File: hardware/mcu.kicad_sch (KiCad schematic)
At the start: 26 parts, among them J5 Conn_ARM_JTAG_SWD_10, SW3 SW_Push, U2 EFR32FG28A122F1024GM48-A, U20 USBLC6-2P6, U21 USBLC6-2P6, X1 HF_Crystal, Y1 LF_Crystal

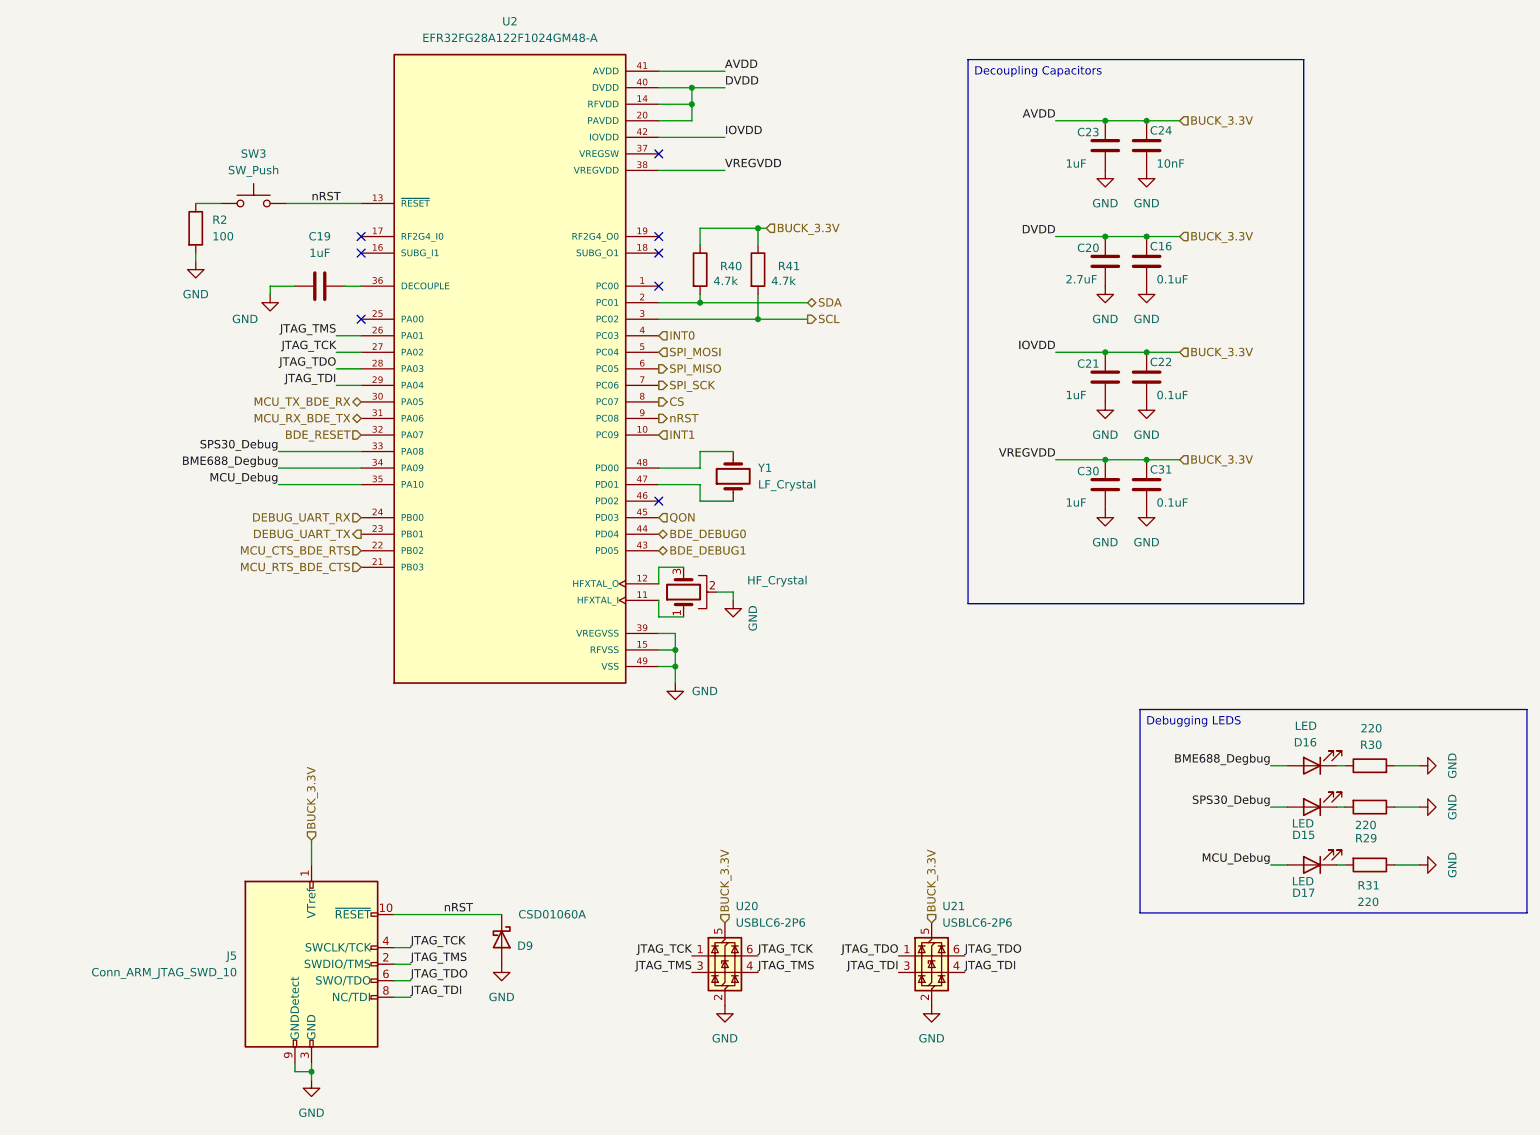
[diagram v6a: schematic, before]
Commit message: Replaced 3.3V symbol
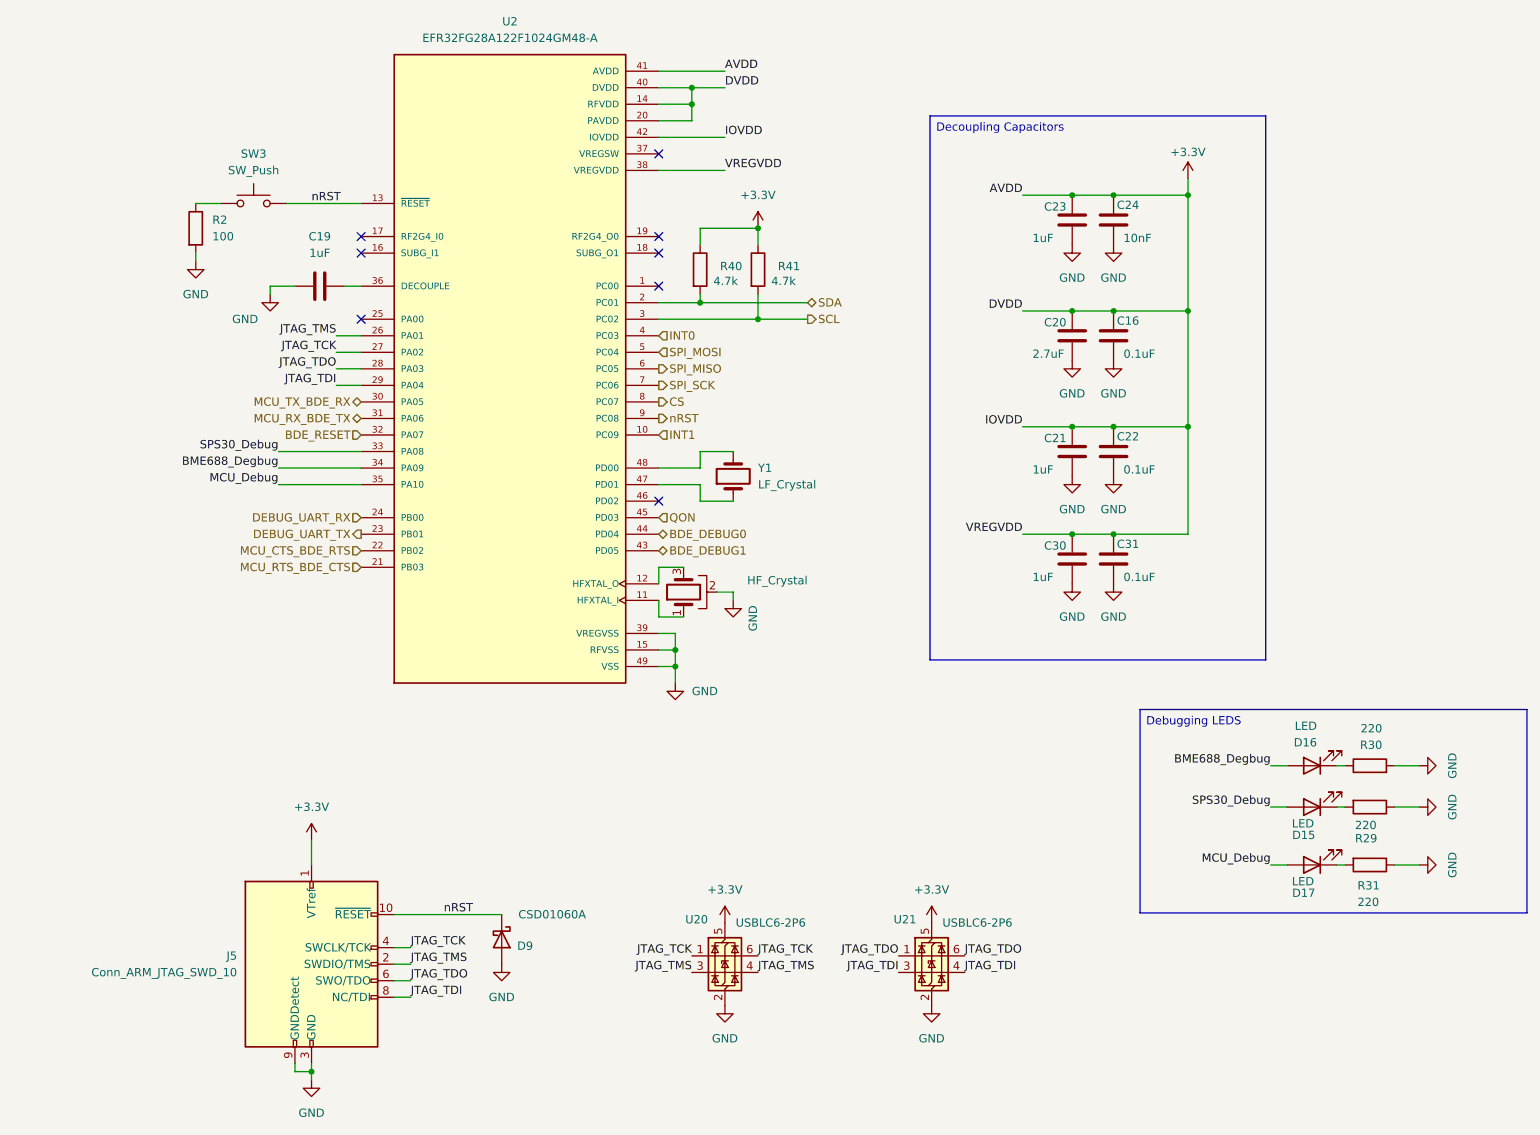
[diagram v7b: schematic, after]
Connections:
- net BUCK_3.3V renamed +3.3V
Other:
- moved on the sheet: C16, C20, C21, C22, C23, C24, C30, C31

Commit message: updated major symbol and footprints
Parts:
- U2: footprint Custom_Parts:QFN40P600X600X90-49N -> pyronet_footprints:QFN40P600X600X90-49N; symbol EFR32FG28A122F1024GM48-A:EFR32FG28A122F1024GM48-A -> pyronet_symbols:EFR32FG28A122F1024GM48-A; Purchase-URL (none) -> https://www.snapeda.com/api/url_track_click_mouser/?unipart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
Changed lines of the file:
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@@
 	)
 	(symbol
-		(lib_id "EFR32FG28A122F1024GM48-A:EFR32FG28A122F1024GM48-A")
+		(lib_id "pyronet_symbols:EFR32FG28A122F1024GM48-A")
 		(at 86.36 72.39 0)
 		(unit 1)
@@
 			)
 		)
-		(property "Footprint" "Custom_Parts:QFN40P600X600X90-49N"
+		(property "Footprint" "pyronet_footprints:QFN40P600X600X90-49N"
 			(at 86.36 72.39 0)
 			(effects
@@
 			(at 86.36 72.39 0)
 			(effects
+				(font
+					(size 1.27 1.27)
+				)
+				(justify bottom)
+				(hide yes)
+			)
+		)
+		(property "Purchase-URL" "https://www.snapeda.com/api/url_track_click_mouser/?unipart_id=15826228&manufacturer=Silicon Laboratories&part_name=EFR32FG28A122F1024GM48-A&search_term=efr32fg28a122f1024gm48-a"
+			(at 86.36 72.39 0)
+			(effects
